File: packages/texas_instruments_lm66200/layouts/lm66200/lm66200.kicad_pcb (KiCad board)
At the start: 2 copper layers, 4 parts

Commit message: WIP update lm66200
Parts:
- C1, C2, C3: footprint atopile:C0402-b3ef17 -> Samsung_Electro_Mechanics_CL05B104KO5NNNC:C0402
- U1: footprint atopile:SOT-583-8_L2.1-W1.2-P0.50-LS1.6-BL-f9e8a4 -> Texas_Instruments_LM66200DRLR:SOT-583-8_L2.1-W1.2-P0.50-LS1.6-BL

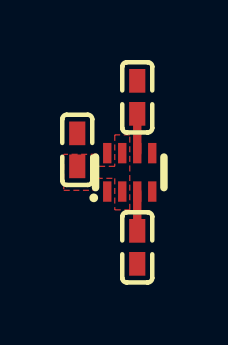
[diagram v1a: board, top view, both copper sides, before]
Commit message: Update 3D model locations
fix missing renders
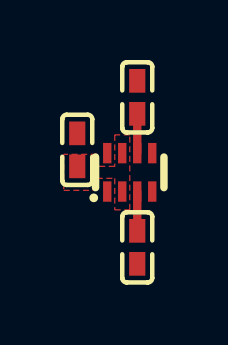
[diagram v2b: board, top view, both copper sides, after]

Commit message: rebuild all packages & regenerate images of changed layouts (silk)
Add new scripts for version bump and build (based on atopile/packages)
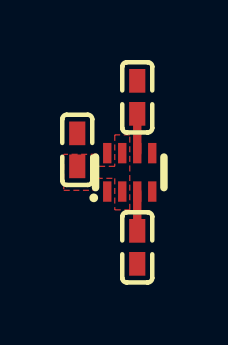
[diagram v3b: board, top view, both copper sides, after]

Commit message: fix lm66200 frozen build
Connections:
- net ONh renamed nON
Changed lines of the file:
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@@
     (net 0 "")
     (net 1 "ST")
-    (net 2 "ONh")
+    (net 2 "nON")
     (net 3 "VOUT")
     (net 4 "hv")
@@
             (size 0.28 0.68)
             (layers "F.Cu" "F.Paste" "F.Mask")
-            (net 2 "ONh")
+            (net 2 "nON")
         )
         (pad "5" smd rect
